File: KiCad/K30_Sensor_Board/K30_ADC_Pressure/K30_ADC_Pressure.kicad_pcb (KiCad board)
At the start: 2 copper layers, 100 x 50.8 mm, 156 parts, among them J1 CONN_02X12, J2 CONN_01X03, J3 CONN_01X05, J4 CONN_01X03, U1 ADS1015_VSSOP, U2 LPS25HB_HLGA

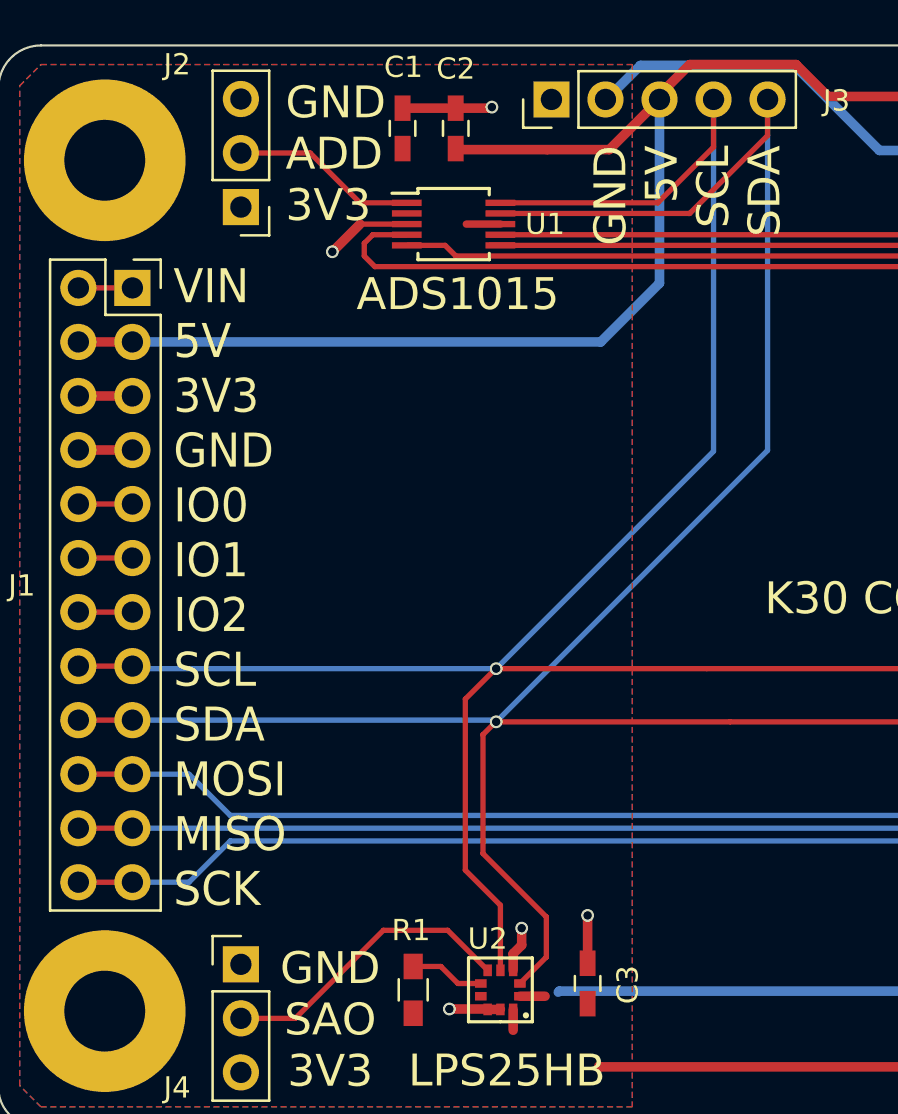
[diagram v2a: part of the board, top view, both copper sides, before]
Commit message: added decoupling capacitors for power input
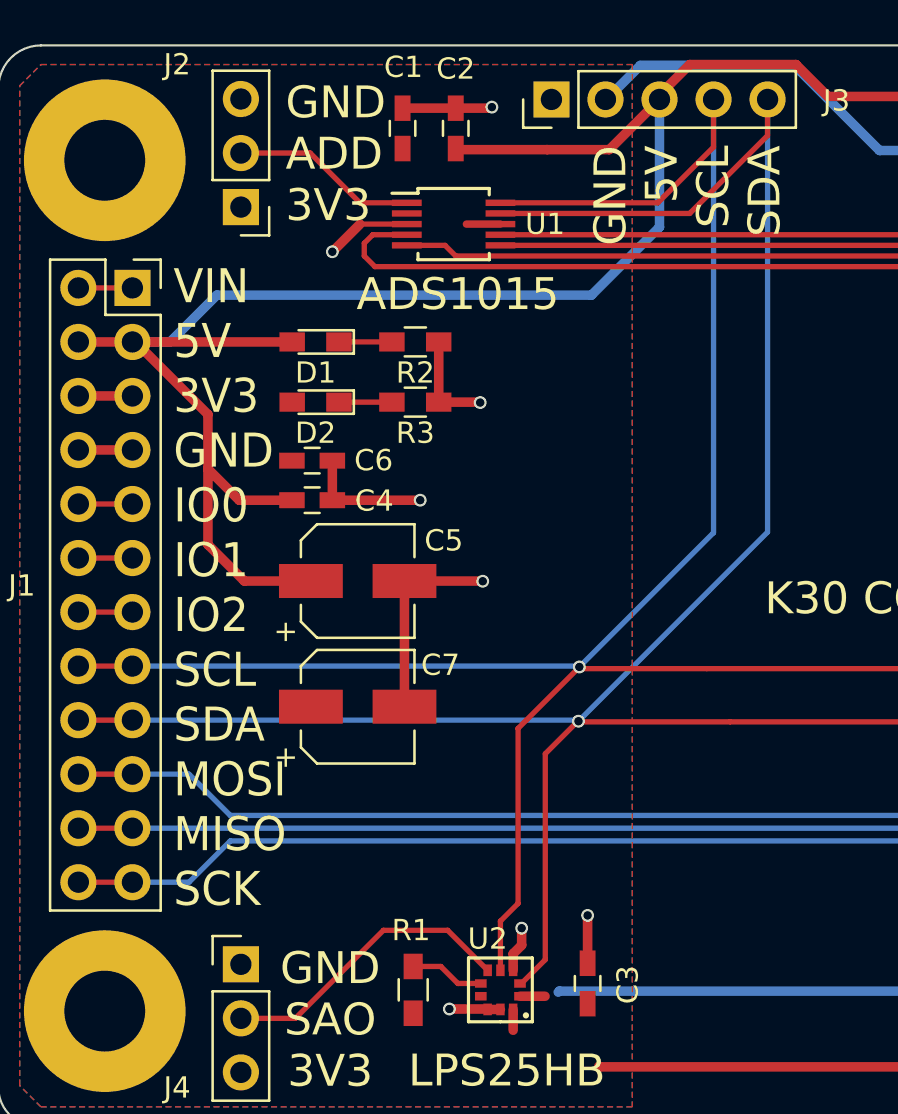
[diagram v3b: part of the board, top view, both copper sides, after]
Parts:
- added C4: 0.1u, Capacitors_SMD:C_0603_HandSoldering, F.Cu at (110.3, 96.6)
- added C5: 10u, Capacitors_SMD:CP_Elec_5x4.5, F.Cu at (112.5, 100.4)
- added C6: 0.1u, Capacitors_SMD:C_0603_HandSoldering, F.Cu at (110.3, 94.7)
- added C7: 10u, Capacitors_SMD:CP_Elec_5x4.5, F.Cu at (112.5, 106.3)
- added D1: LED, LEDs:LED_0603_HandSoldering, F.Cu at (110.5, 89.1)
- added D2: LED, LEDs:LED_0603_HandSoldering, F.Cu at (110.5, 92.0)
- added R2: 2.2k, Resistors_SMD:R_0603_HandSoldering, F.Cu at (115.2, 89.1)
- added R3: 2.2k, Resistors_SMD:R_0603_HandSoldering, F.Cu at (115.2, 92.0)
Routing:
- net /5V: track 106.5 -> 133.6 mm
- net GND: track 142.9 -> 163.0 mm, vias 5 -> 8
- net Net-(D2-Pad1): track 0.00 -> 2.49 mm
- net Net-(D1-Pad1): track 0.00 -> 2.49 mm
- net /SDA: track 141.2 -> 138.8 mm
- net /SCL: track 136.3 -> 135.1 mm

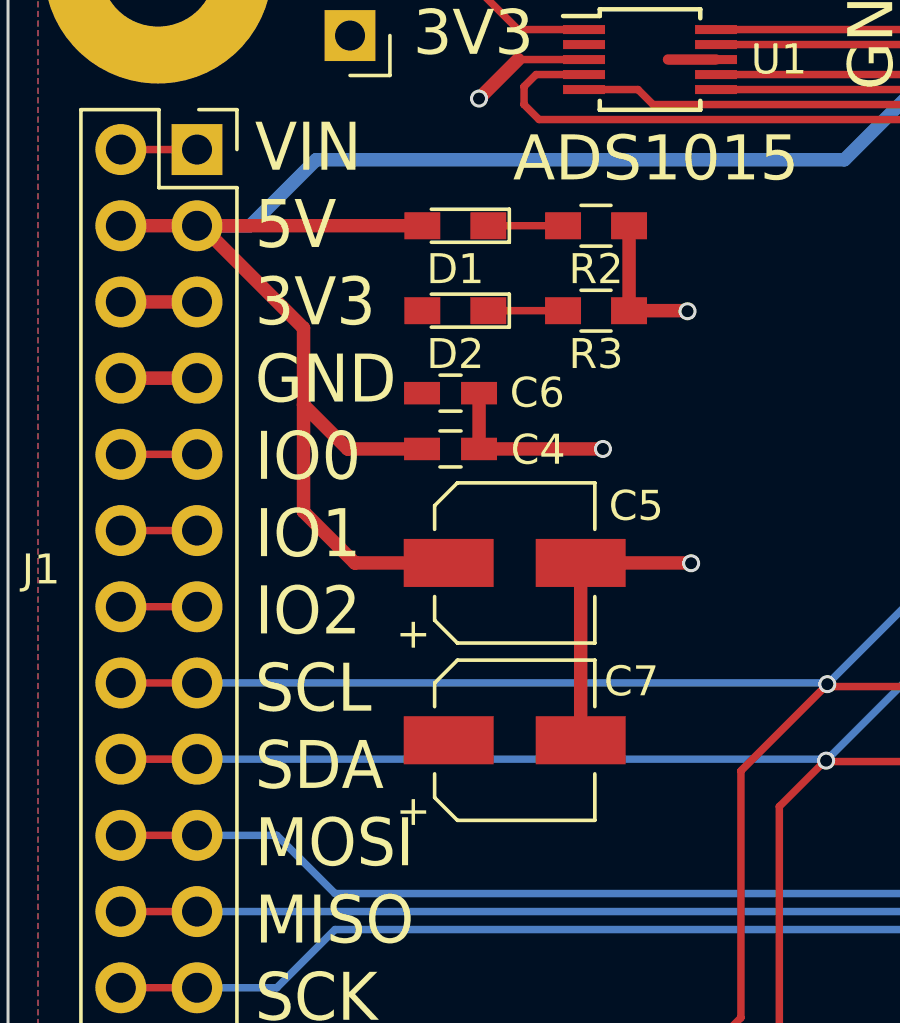
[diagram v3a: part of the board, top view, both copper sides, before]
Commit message: remove leds, new gerber files
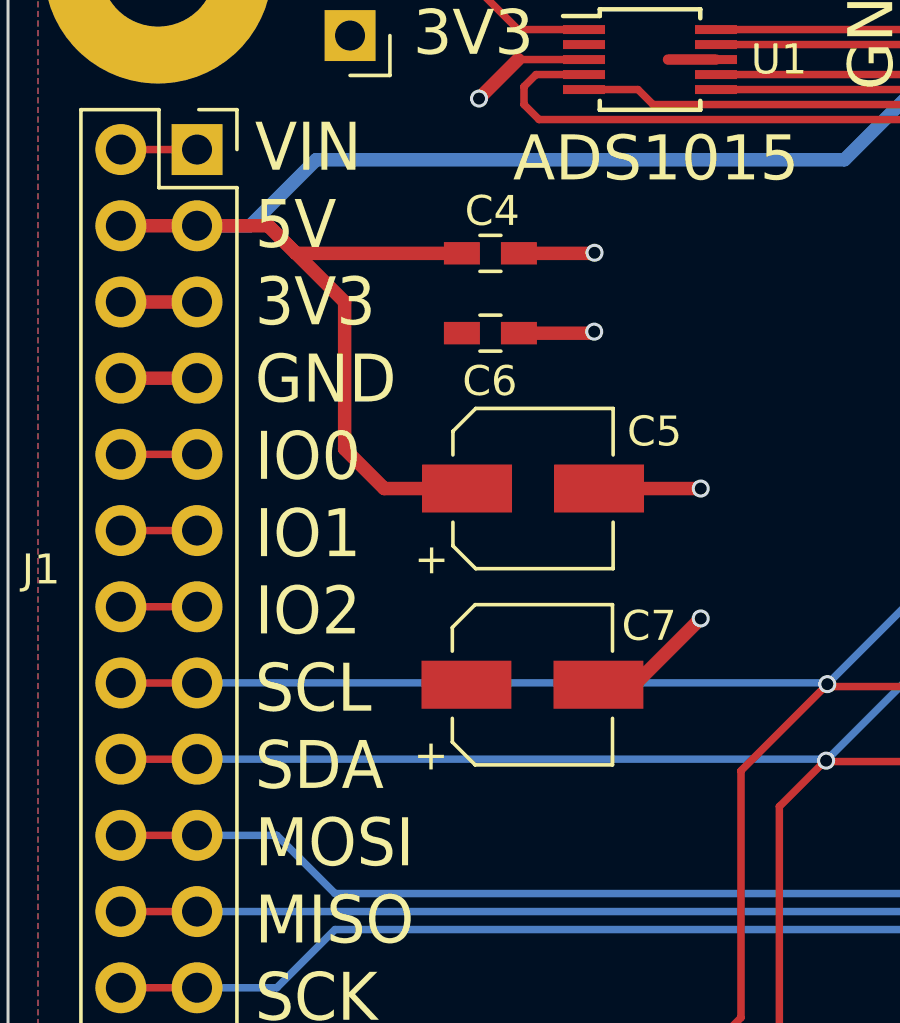
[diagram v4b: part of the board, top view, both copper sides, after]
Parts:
- removed D1, D2: LED, LEDs:LED_0603_HandSoldering
- removed R2, R3: 2.2k, Resistors_SMD:R_0603_HandSoldering
- moved C4 6.65 mm to (111.7, 90.1)
- moved C5 2.55 mm to (113.1, 97.9)
- moved C6 2.40 mm to (111.7, 92.7)
- moved C7 1.94 mm to (113.1, 104.4)
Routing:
- net GND: track 163.0 -> 155.7 mm, vias 8 -> 9
- net /5V: track 133.6 -> 127.4 mm
- net Net-(D2-Pad1): track 2.49 -> 0.00 mm
- net Net-(D1-Pad1): track 2.49 -> 0.00 mm
